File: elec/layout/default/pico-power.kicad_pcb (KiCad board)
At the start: 2 copper layers, 225.7 x 100.8 mm, 0 parts

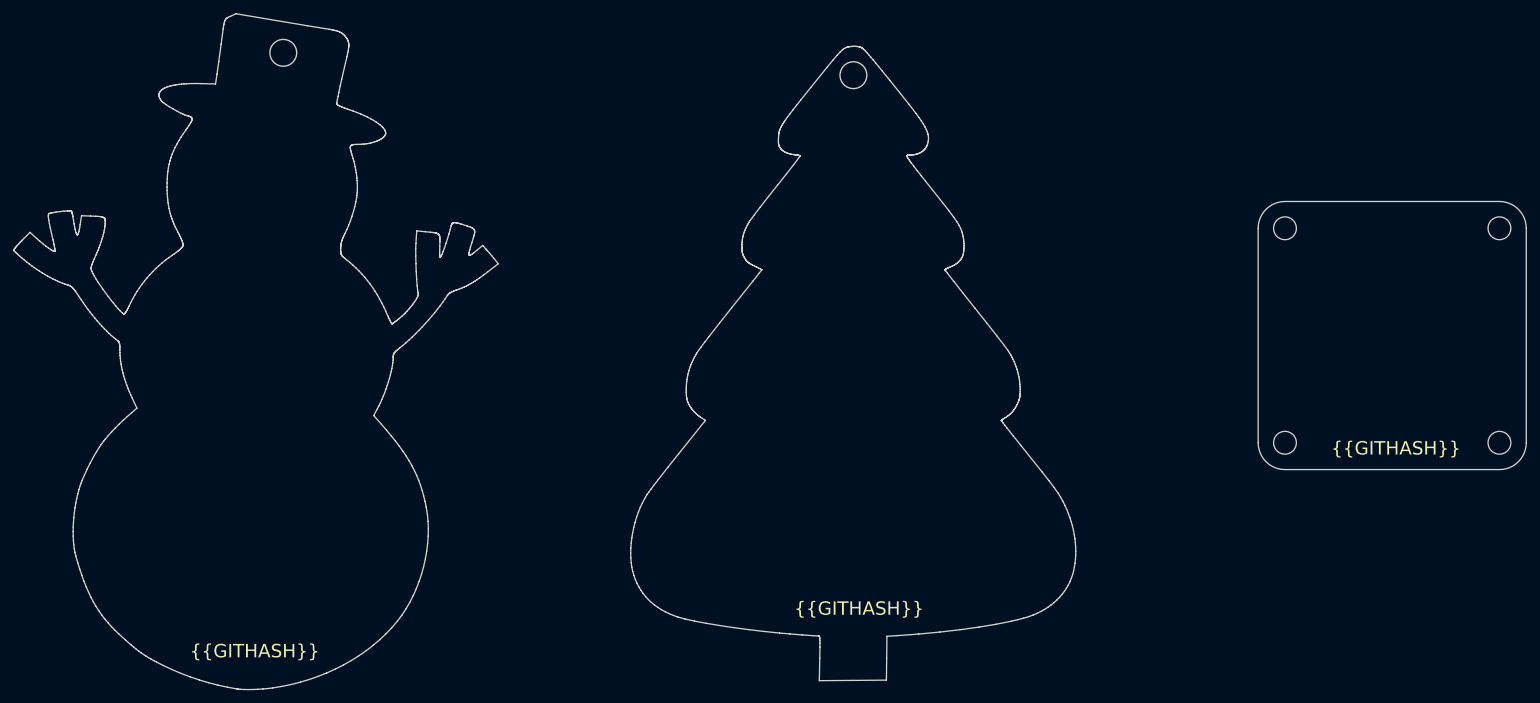
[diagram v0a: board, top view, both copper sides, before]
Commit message: demo board ready to build
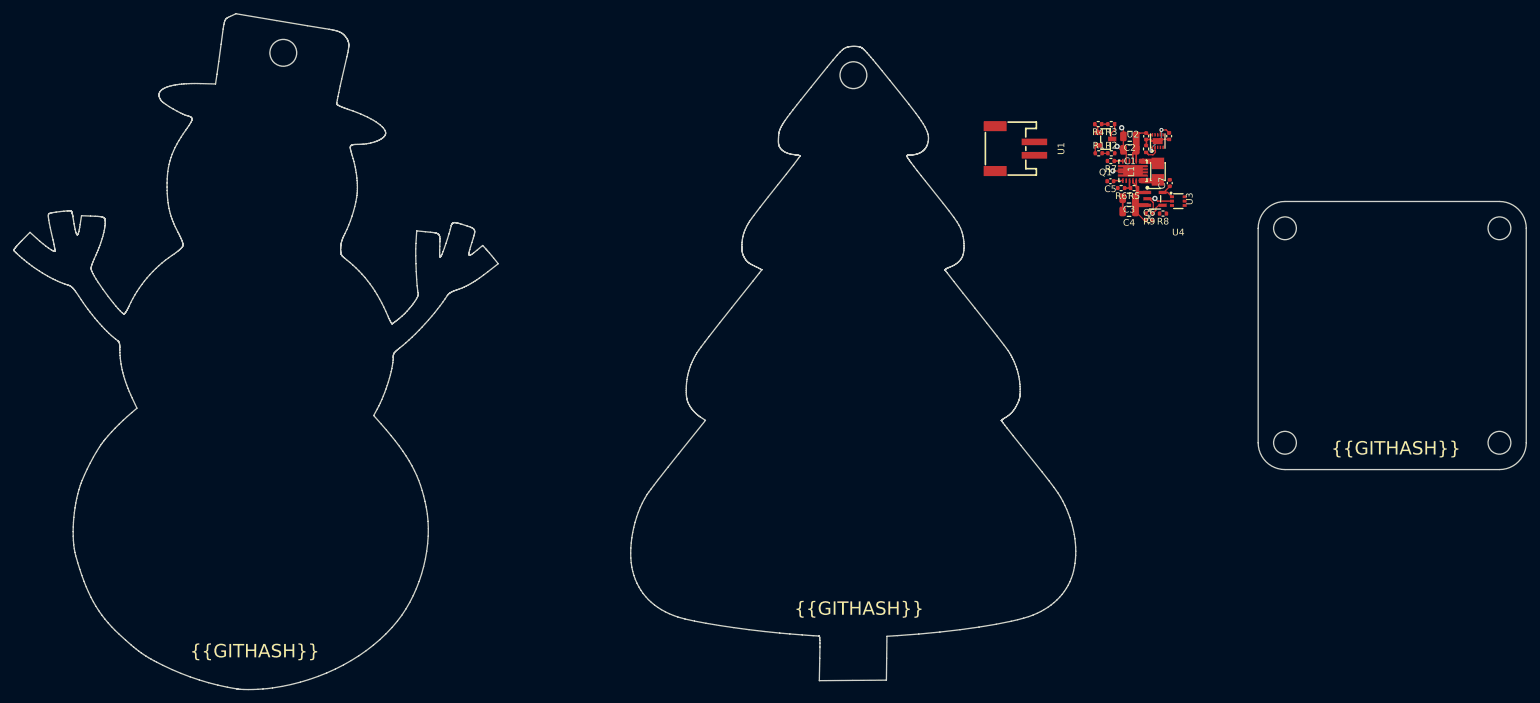
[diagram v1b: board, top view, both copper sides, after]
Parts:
- added C1: 25V 10uF X5R ±10% 0805 Multilayer Ceramic Capacitors MLCC -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, lib:C0805, F.Cu at (202.5, 70.1)
- added C2: 25V 10uF X5R ±10% 0805 Multilayer Ceramic Capacitors MLCC -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, lib:C0805, F.Cu at (202.5, 68.1)
- added C3: 25V 10uF X5R ±10% 0805 Multilayer Ceramic Capacitors MLCC -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, lib:C0805, F.Cu at (202.3, 77.3)
- added C4: 25V 10uF X5R ±10% 0805 Multilayer Ceramic Capacitors MLCC -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, lib:C0805, F.Cu at (202.4, 79.3)
- added C5: 16V 100nF X7R ±10% 0402 Multilayer Ceramic Capacitors MLCC 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, lib:C0402, F.Cu at (199.6, 74.8)
- added C6: 25V 1uF X5R ±10% 0402 Multilayer Ceramic Capacitors MLCC - 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, lib:C0402, F.Cu at (205.4, 80.6)
- added C7: 25V 1uF X5R ±10% 0402 Multilayer Ceramic Capacitors MLCC - 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, lib:C0402, F.Cu at (208.4, 75.0)
- added C8: 25V 1uF X5R ±10% 0402 Multilayer Ceramic Capacitors MLCC - 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, lib:C0402, F.Cu at (208.3, 68.0)
- added C9: 25V 1uF X5R ±10% 0402 Multilayer Ceramic Capacitors MLCC - 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, lib:C0402, F.Cu at (204.9, 68.1)
- added L1: , lib:IND-SMD_L2.5-W2.0_WPN252012H, F.Cu at (206.7, 73.3)
- added Q1: , lib:SOT-23-3_L2.9-W1.3-P1.90-LS2.4-BR, F.Cu at (198.8, 68.5)
- added R1: 62.5mW Thick Film Resistors 50V ±100ppm/℃ ±1% 107Ω 0402 Chi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, lib:R0402, F.Cu at (197.8, 70.6)
- added R10: 62.5mW Thick Film Resistors 75V ±1% ±100ppm/℃ 576Ω 0402 Chi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, lib:R0402, F.Cu at (204.9, 70.0)
- added R2: 62.5mW Thick Film Resistors 50V ±100ppm/℃ ±5% 360Ω 0402 Chi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, lib:R0402, F.Cu at (199.7, 70.6)
- added R3: 62.5mW Thick Film Resistors 50V ±100ppm/℃ ±1% 100kΩ 0402 Ch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, lib:R0402, F.Cu at (199.7, 66.2)
- added R4: 62.5mW Thick Film Resistors 50V ±1% ±200ppm/℃ 100Ω 0402 Chi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, lib:R0402, F.Cu at (197.8, 66.2)
- added R5: 62.5mW Thick Film Resistors 50V ±100ppm/℃ ±1% 24.3kΩ 0402 C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, lib:R0402, F.Cu at (203.1, 75.8)
- added R6: 62.5mW Thick Film Resistors 50V ±100ppm/℃ ±1% 4.02kΩ 0402 C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, lib:R0402, F.Cu at (201.2, 75.8)
- added R7: 62.5mW Thick Film Resistors 50V ±100ppm/℃ ±1% 1MΩ 0402 Chip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, lib:R0402, F.Cu at (199.6, 71.8)
- added R8: 62.5mW Thick Film Resistors ±100ppm/℃ ±1% 17.4kΩ 0402 Chip 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, lib:R0402, F.Cu at (207.4, 79.6)
- added R9: 62.5mW Thick Film Resistors 50V ±100ppm/℃ ±1% 10.2kΩ 0402 C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, lib:R0402, F.Cu at (205.4, 79.6)
- added U1: , lib:CONN-SMD_P2.00_S2B-PH-SM4-TB-LF-SN, F.Cu at (185.3, 69.9)
- added U2: , lib:VSON-14_L4.0-W3.0-P0.50-BL-EP_TI_DSJ, F.Cu at (202.9, 73.2)
- added U3: , lib:SOT-23-5_L3.0-W1.7-P0.95-LS2.8-BL, F.Cu at (206.2, 77.4)
- added U4: , lib:SC-70-6_L2.2-W1.3-P0.65-LS2.1-BR, F.Cu at (209.7, 77.7)
- added U5: , lib:WSON-10_L2.0-W2.0-P0.40-BL-EP, F.Cu at (206.6, 68.8)
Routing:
- net gnd: track 0.00 -> 23.2 mm, vias 0 -> 4
- net buck_boost-vcc: track 0.00 -> 12.1 mm
- net battery-vcc: track 0.00 -> 11.0 mm
- net vcc-2: track 0.00 -> 6.47 mm, vias 0 -> 2
- net vcc: track 0.00 -> 3.09 mm
- net iset: track 0.00 -> 2.76 mm
- net l1: track 0.00 -> 2.59 mm
- net l2: track 0.00 -> 2.54 mm
- net ldo.feedback_div-out: track 0.00 -> 2.21 mm
- net buck_boost.feedback_div-out: track 0.00 -> 2.08 mm
- net battery_vdiv.pfet-gnd: track 0.00 -> 1.49 mm
- net vina: track 0.00 -> 1.41 mm
- net battery_vdiv.pfet-vcc: track 0.00 -> 1.29 mm
- net buck_boost.ic-pg: track 0.00 -> 1.29 mm
- net vcc-5: track 0.00 -> 0.92 mm
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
